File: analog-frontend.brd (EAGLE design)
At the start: 26.7 x 25.1 mm, 67 parts, among them IC1 ADG731, IC2 TPS63031, IC3 INA332, IC4 OPA2320, IC5 TM4C123G, IC6 NRF24L01SMD, Y1 CRYSTAL3X2, Y2 CRYSTAL3X2

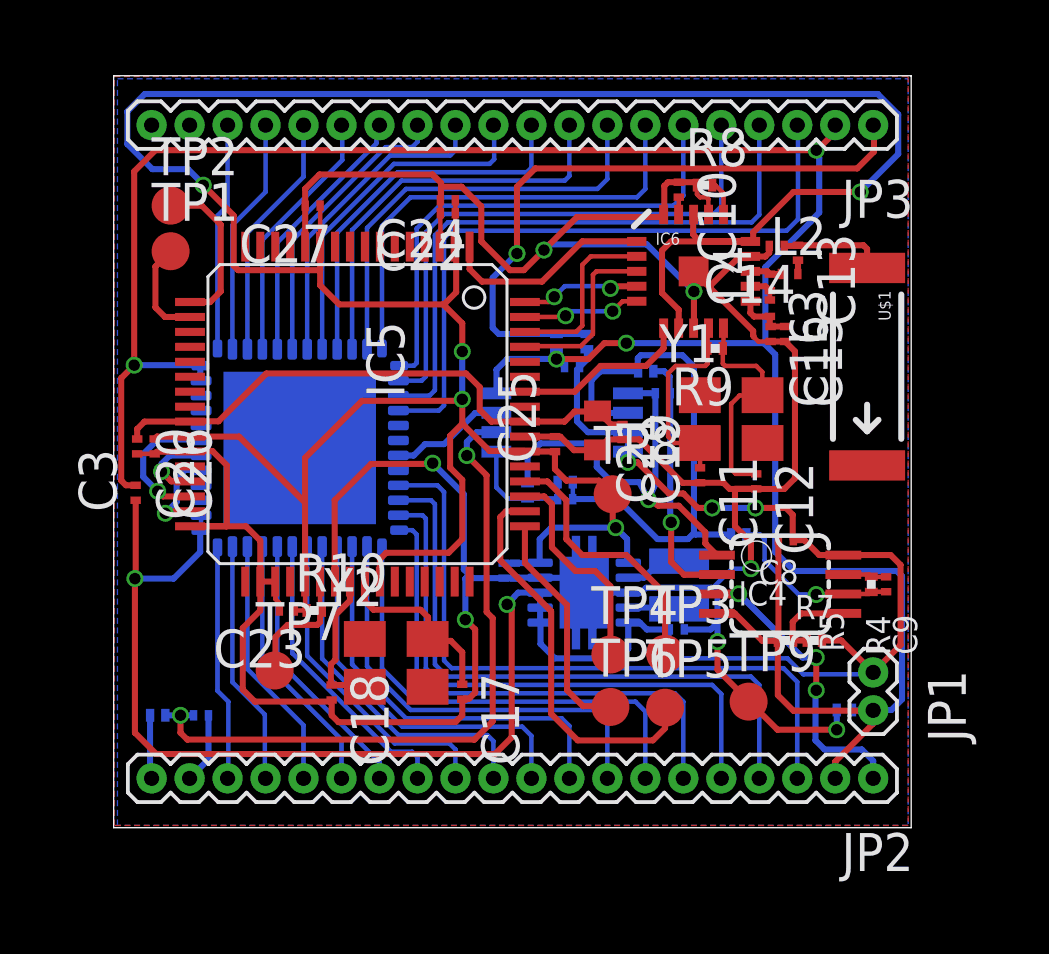
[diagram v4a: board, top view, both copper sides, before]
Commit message: added signal planes
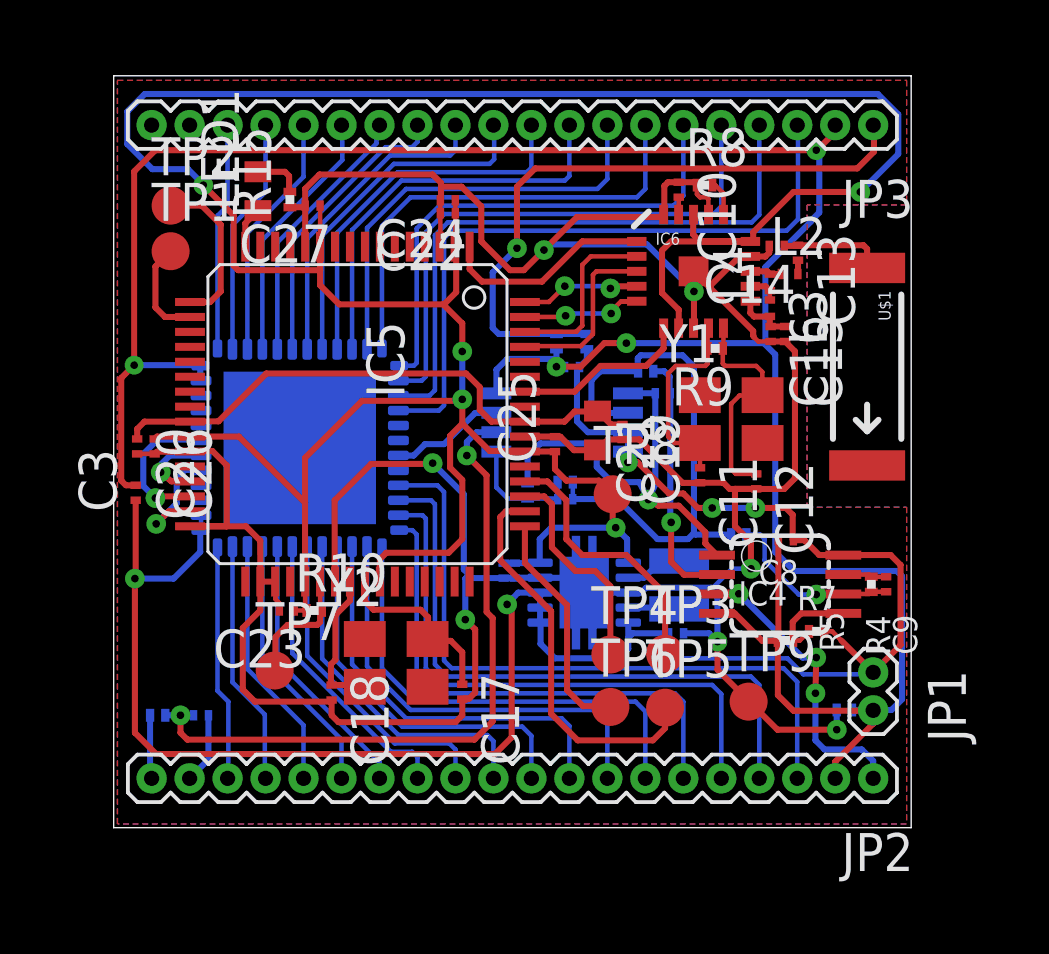
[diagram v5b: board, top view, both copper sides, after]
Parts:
- added LED1: (no value), ng:0402
- added R15: (no value), rcl:R0201
- moved R7 0.31 mm to (23.5, 6.57)
- moved C1 0.13 mm to (18.8, 6.50)
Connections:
- new net N$63: IC5.16, LED1.1
- new net N$66: LED1.2, R15.2
- net GND: now also R15.1
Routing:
- net N$66: track 0.00 -> 1.64 mm
- net N$63: track 0.00 -> 1.38 mm
- net PF3: track 3.12 -> 4.05 mm
- net GND: track 116.3 -> 115.6 mm
- net N$58: track 3.96 -> 4.47 mm

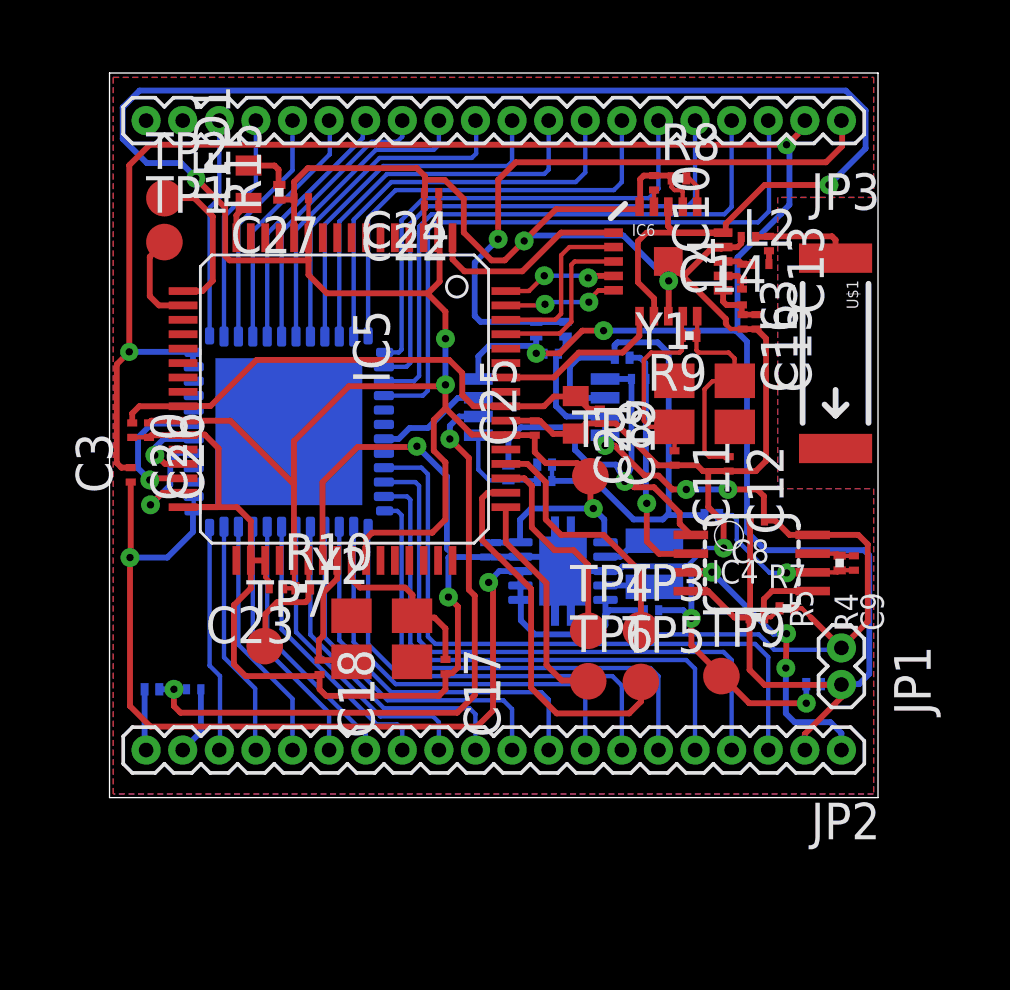
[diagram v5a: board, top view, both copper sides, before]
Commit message: fixed analog input connection
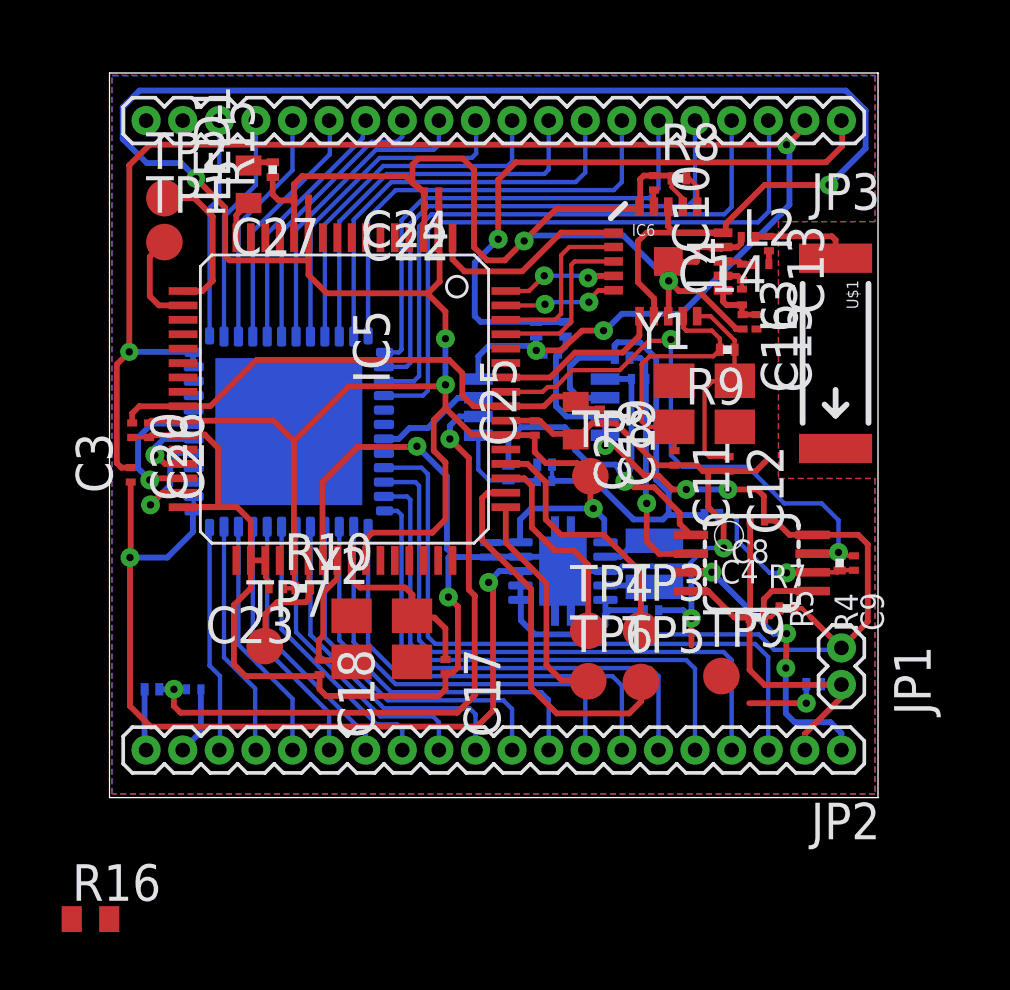
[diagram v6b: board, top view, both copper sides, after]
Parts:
- added R16: (no value), FAB_Hello:0402
- moved R9 1.41 mm to (21.4, 15.5)
- moved R15 0.82 mm to (5.66, 21.8)
- moved C21 0.20 mm to (16.2, 13.1)
- moved C27 0.05 mm to (6.65, 20.8)
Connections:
- removed net N$41: C9.1, IC4.7, R4.1
- new net AIN: C9.1, IC4.7, IC5.57, R4.1
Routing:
- net AIN: track 0.00 -> 19.9 mm, vias 0 -> 2
- net GNDA: track 87.8 -> 69.2 mm
- net GND: track 115.6 -> 111.0 mm
- net N$46: track 6.75 -> 9.21 mm
- net N$41: track 1.46 -> 0.00 mm
- net N$66: track 1.64 -> 0.89 mm
- net +3V3: track 107.0 -> 106.4 mm

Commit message: Revert "fixed analog input connection"
This reverts commit 9ace190f50edbfe5c6ebec0060ae9832deedc051.
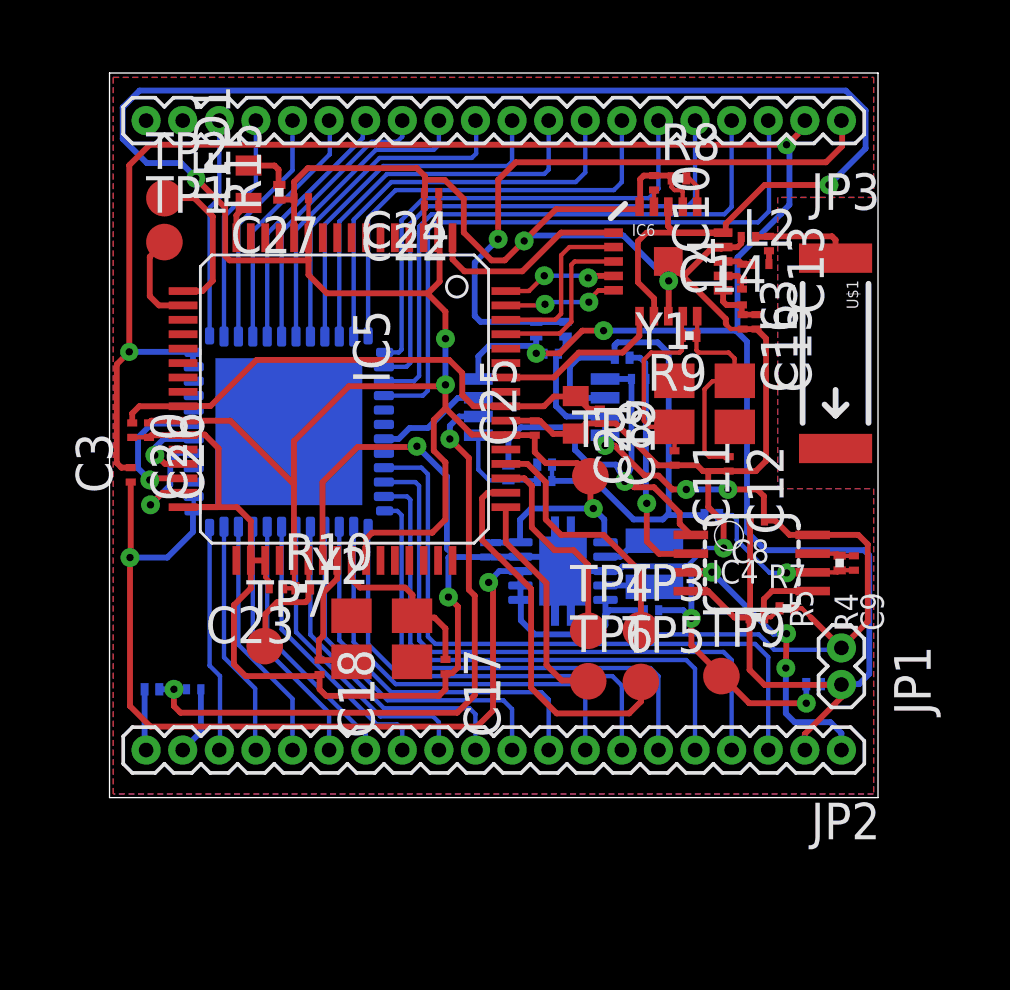
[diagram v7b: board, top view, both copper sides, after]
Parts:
- removed R16: (no value), FAB_Hello:0402
- moved R9 1.41 mm to (20.1, 16.0)
- moved R15 0.82 mm to (5.89, 21.0)
- moved C21 0.20 mm to (16.2, 13.3)
- moved C27 0.05 mm to (6.65, 20.8)
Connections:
- removed net AIN: C9.1, IC4.7, IC5.57, R4.1
- new net N$41: C9.1, IC4.7, R4.1
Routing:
- net AIN: track 19.9 -> 0.00 mm, vias 2 -> 0
- net GNDA: track 69.2 -> 87.8 mm
- net GND: track 111.0 -> 115.6 mm
- net N$46: track 9.21 -> 6.75 mm
- net N$41: track 0.00 -> 1.46 mm
- net N$66: track 0.89 -> 1.64 mm
- net +3V3: track 106.4 -> 107.0 mm

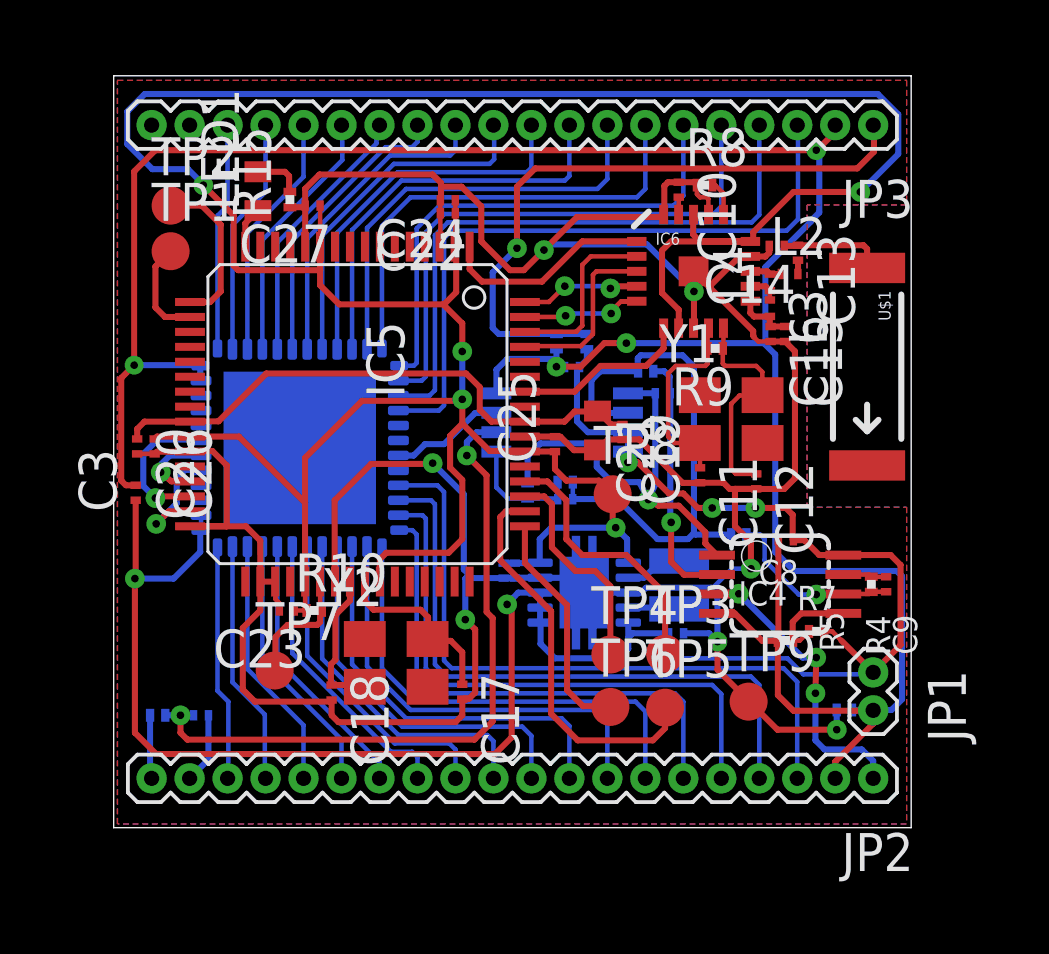
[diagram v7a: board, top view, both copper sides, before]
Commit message: changed all components to 0402
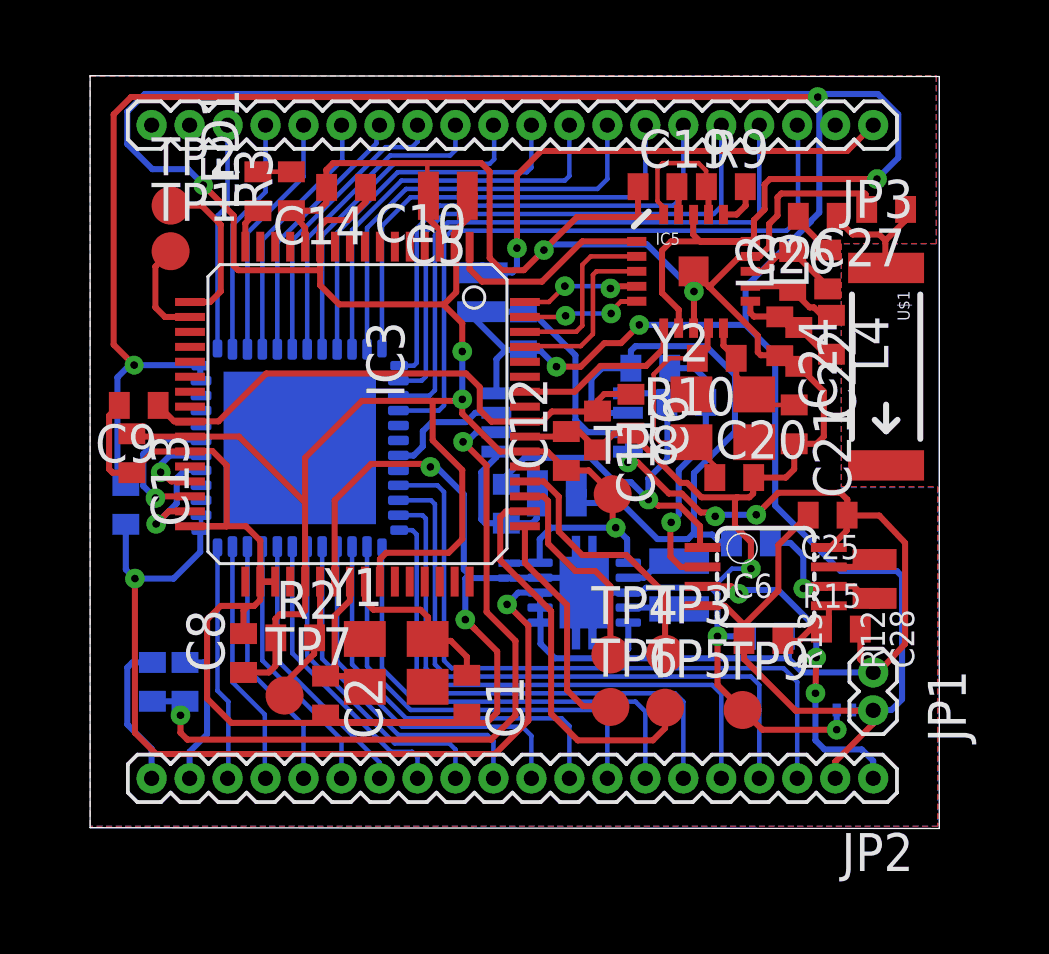
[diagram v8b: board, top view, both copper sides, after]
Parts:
- C1, C10, C11, C12, C13, C14, C15, C16, C17, C18, C19, C2, C20, C22, C23, C24, C25, C26, C27, C28, C3, C5, C6, C8, C9: device rcl:C0201 -> rcl:C0402
- IC1: value ADG731 -> TPS63031; device mor307:LFCSP48 -> mor307:S-PDSO-N10
- IC2: value TPS63031 -> ADG731; device mor307:S-PDSO-N10 -> mor307:LFCSP48
- IC3: value INA332 -> TM4C123G; device mor307:DGK_S-PDSO-G8 -> mor307:LQFP64
- IC4: value OPA2320 -> INA332; device mor307:MSOP08 -> mor307:DGK_S-PDSO-G8
- IC5: value TM4C123G -> NRF24L01SMD; device mor307:LQFP64 -> SparkFun-RF:QFN20
- IC6: value NRF24L01SMD -> OPA2320; device SparkFun-RF:QFN20 -> mor307:MSOP08
- L2, L3, L4: device rcl:L0201 -> rcl:R0402
- R10, R11, R12, R13, R14, R15, R2, R3, R4, R5, R6, R7, R8, R9: device rcl:R0201 -> rcl:R0402
- moved C9 25.7 mm to (0.84, 14.1), turned to 180 degrees
- moved R4 24.3 mm to (1.30, 4.88), flipped to the bottom, turned to 90 degrees
- moved C26 23.5 mm to (23.5, 20.4), turned to 180 degrees
- moved R15 23.4 mm to (24.3, 6.64), turned to 180 degrees
- moved C13 23.3 mm to (0.61, 12.5)
- moved C28 23.3 mm to (25.7, 8.32), flipped to the top, turned to 270 degrees
- moved C16 22.8 mm to (2.39, 4.88), flipped to the bottom, turned to 90 degrees
- moved C15 22.8 mm to (0.41, 10.8), flipped to the bottom, turned to 90 degrees
- moved C3 21.6 mm to (21.8, 6.40), flipped to the bottom, turned to 0 degrees
- moved R14 20.7 mm to (21.3, 9.53)
- moved C20 20.0 mm to (20.8, 11.7), turned to 0 degrees
- moved C27 19.2 mm to (25.8, 20.7)
- moved C8 18.5 mm to (4.34, 5.84), turned to 90 degrees
- moved R10 15.9 mm to (20.2, 15.7), turned to 180 degrees
- moved R5 15.2 mm to (12.7, 17.9), flipped to the bottom, turned to 90 degrees
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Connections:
- net +3V3: now also C10.1, C12.1, C13.1, C14.1, C5.1, C7.1, C8.1, IC1.1, IC1.10, IC3.11, IC3.2, IC3.26, IC3.37, IC3.42, IC3.54, IC5.15, IC5.18, IC5.7, R2.1; no longer C2.1, C22.1, C23.1, C24.1, C25.1, C26.1, C27.1, IC2.1, IC2.10, IC5.11, IC5.2, IC5.26, IC5.37, IC5.42, IC5.54, IC6.15, IC6.18, IC6.7, R10.1
- net GND: now also C10.2, C13.2, C19.1, C3.2, C5.2, C6.2, C7.2, C8.2, C9.2, IC1.3, IC1.9, IC3.12, IC3.27, IC3.3, IC3.32, IC3.34, IC3.35, IC3.39, IC3.55, IC5.0, IC5.14, IC5.17, IC5.20, IC5.8, R1.2, R3.1, R9.1; no longer C10.1, C15.2, C16.2, C17.2, C18.2, C19.2, C23.2, C25.2, C26.2, IC2.3, IC2.9, IC5.12, IC5.27, IC5.3, IC5.32, IC5.34, IC5.35, IC5.39, IC5.55, IC6.0, IC6.14, IC6.17, IC6.20, IC6.8, R13.2, R15.1, R8.1
- net GNDA: now also C15.2, C17.1, C25.1, IC2.23, IC2.24, IC6.4, R1.1, R8.2; no longer C3.2, C5.1, C8.1, IC1.23, IC1.24, IC3.4, R12.2, R5.1
- net N$1: now also IC2.12; no longer IC1.12
- net N$10: now also IC2.6; no longer IC1.6
- net N$11: now also IC2.5; no longer IC1.5
- net N$12: now also IC2.4; no longer IC1.4
- net N$13: now also IC2.3; no longer IC1.3
- net N$14: now also IC2.2; no longer IC1.2
- net N$15: now also IC2.1; no longer IC1.1
- net N$16: now also IC2.48; no longer IC1.48
- net N$17: now also IC2.47; no longer IC1.47
- net N$18: now also IC2.46; no longer IC1.46
- net N$19: now also IC2.26; no longer IC1.26
- net N$2: now also IC2.45; no longer IC1.45
- net N$20: now also IC2.27; no longer IC1.27
- net N$21: now also IC2.28; no longer IC1.28
- net N$22: now also IC2.29; no longer IC1.29
- net N$23: now also IC2.30; no longer IC1.30
- net N$24: now also IC2.31; no longer IC1.31
- net N$25: now also IC2.32; no longer IC1.32
- net N$26: now also IC2.33; no longer IC1.33
- net N$27: now also IC2.34; no longer IC1.34
- net N$28: now also IC2.35; no longer IC1.35
- net N$29: now also IC2.36; no longer IC1.36
- net N$3: now also IC2.25; no longer IC1.25
- net N$30: now also IC2.37; no longer IC1.37
- net N$31: now also IC2.38; no longer IC1.38
- net N$32: now also IC2.39; no longer IC1.39
- net N$33: now also IC1.4; no longer IC2.4
- net N$34: now also IC1.2; no longer IC2.2
- net N$35: now also IC2.43, IC4.3; no longer IC1.43, IC3.3
- net N$36: now also C23.1, IC4.5, IC6.1, R7.2; no longer C7.1, IC3.5, IC4.1, R2.2
- net N$37: now also C2.1, IC3.40, Y1.1; no longer C18.1, IC5.40, Y2.1
- net N$38: now also C18.1, IC4.1, R6.1, R7.1; no longer C6.1, IC3.1, R1.1, R2.1
- net N$39: now also C28.2, IC6.6, R12.2, R14.1; no longer C9.2, IC4.6, R4.2, R6.1
- net N$4: now also IC2.40; no longer IC1.40
- net N$40: now also C1.1, IC3.41, Y1.3; no longer C17.1, IC5.41, Y2.3
- net N$41: now also C28.1, IC6.7, R12.1; no longer C9.1, IC4.7, R4.1
- net N$42: now also C23.2, IC6.2, R11.2; no longer C7.2, IC4.2, R3.2
- net N$43: now also C19.2, IC5.19; no longer C10.2, IC6.19
- net N$44: now also IC5.16, R9.2; no longer IC6.16, R8.2
- net N$45: now also C11.1, C6.1, C9.1, IC3.25, IC3.56; no longer C19.1, C20.1, C21.1, IC5.25, IC5.56
- net N$46: now also C20.1, IC5.9, R10.2, Y2.1; no longer C11.1, IC6.9, R9.2, Y1.1
- net N$47: now also IC6.5, R13.2, R15.2; no longer IC4.5, R5.2, R7.2
- net N$48: now also C21.1, IC5.10, R10.1, Y2.3; no longer C12.1, IC6.10, R9.1, Y1.3
- net N$49: now also IC3.38, R2.2; no longer IC5.38, R10.2
- net N$5: now also IC2.11; no longer IC1.11
- net N$50: now also IC5.12, L2.1; no longer IC6.12, L3.1
- net N$51: now also IC5.13, L2.2, L3.1; no longer IC6.13, L2.1, L4.2
- net N$52: now also C22.1, C24.1, IC5.11, L4.2; no longer C15.1, C16.1, IC6.11, L3.2
- net N$53: now also C26.2, L3.2; no longer C13.2, L2.2
- net N$54: now also C26.1, C27.1; no longer C13.1, C14.1
- net N$55: now also IC3.61, IC5.3; no longer IC5.61, IC6.3
- net N$56: now also IC3.62, IC5.2; no longer IC5.62, IC6.2
- net N$58: now also IC3.63, IC5.5; no longer IC5.63, IC6.5
- net N$59: now also IC3.1; no longer IC6.1
- net N$6: now also IC2.10; no longer IC1.10
- net N$60: now also IC3.58, IC5.6; no longer IC5.58, IC6.6
- net N$61: now also IC3.64, IC5.4; no longer IC5.64, IC6.4
- net N$62: now also C16.1, IC4.2, R4.1; no longer C28.1, IC3.2, R14.1
- net N$63: now also IC3.16; no longer IC5.16
- net N$66: now also R3.2; no longer R15.2
- net N$7: now also IC2.9; no longer IC1.9
- net N$8: now also IC2.8; no longer IC1.8
- net N$9: now also IC2.7; no longer IC1.7
- net PF1: now also IC2.18, IC3.29; no longer IC1.18, IC5.29
- net PF2: now also IC2.19, IC3.30; no longer IC1.19, IC5.30
- net PF3: now also IC2.17, IC3.31; no longer IC1.17, IC5.31
- net RXD: now also IC3.18; no longer IC5.18
- net TCK: now also IC3.52; no longer IC5.52
- net TDI: now also IC3.50; no longer IC5.50
- net TDO: now also IC3.49; no longer IC5.49
- net TMS: now also IC3.51; no longer IC5.51
- net TXD: now also IC3.17; no longer IC5.17
- net VCM: now also R5.2, R8.1; no longer R11.2, R12.1
- net VCM1: now also IC6.3; no longer IC4.3
- net VCM2: now also R4.2; no longer R14.2
- net VDDA: now also C15.1, C17.2, C25.2, IC1.5, IC1.6, IC1.7, IC1.8, IC2.13, IC2.14, IC4.7, IC6.8, R15.1, R5.1; no longer C1.1, C5.2, C8.2, IC1.13, IC1.14, IC2.5, IC2.6, IC2.7, IC2.8, IC3.7, IC3.8, R11.1, R7.1
- net VOUT: now also C18.2, IC4.6, R11.1, R14.2; no longer C6.2, IC3.6, R1.2, R3.1
- net VREF: now also C16.2; no longer C28.2
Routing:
- net GND: track 115.6 -> 142.4 mm
- net +3V3: track 107.0 -> 114.9 mm
- net GNDA: track 87.8 -> 93.3 mm
- net VDDA: track 68.2 -> 73.5 mm
- net VCM: track 22.7 -> 17.4 mm
- net N$48: track 7.67 -> 4.40 mm
- net VCM2: track 2.13 -> 4.95 mm
- net VREF: track 2.37 -> 4.79 mm
- net N$51: track 1.08 -> 3.42 mm
- net VOUT: track 18.4 -> 20.6 mm
- net N$50: track 1.03 -> 3.09 mm
- net N$62: track 23.1 -> 25.0 mm
- net N$52: track 1.93 -> 3.66 mm
- net N$38: track 3.98 -> 5.62 mm
- net N$46: track 6.75 -> 8.29 mm
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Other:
- board size 26.7 x 25.1 mm -> 28.4 x 25.2 mm
